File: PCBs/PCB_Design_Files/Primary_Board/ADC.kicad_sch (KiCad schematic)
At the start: 0 parts

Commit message: update
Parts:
- added U10: 74HC595D, symbol project_symbols:74HC595D
- added U11: TMUX1104DGSR, symbol project_symbols:TMUX1104
- added U7: REF3333AIDBZR, symbol project_symbols:REF3333AIDBZR
- added U8: TMUX1133PWR, symbol project_symbols:TMUX1133PWR
- added U9: MCP6561T-E/OT, symbol project_symbols:MCP6561T-E/OT

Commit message: added some parts of schematic
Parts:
- added C10, C11, C12, C13: 10nF, symbol Device:C_Small
- added C14, C53, C54: 100nF, symbol Device:C_Small
- added C15, C16, C17, C18, C19, C20, C21, C22, C23, C24, C25, C26, C27, C28, C29, C33, C34, C35, C36, C37, C38, C39, C40, C41, C42, C43, C44, C45, C46, C47: 8pF, symbol Device:C_Small
- added C30, C48: 4pF, symbol Device:C_Small
- added C31, C49: 2pF, symbol Device:C_Small
- added C32, C50, C51, C52: 1pF, symbol Device:C_Small
- added R12, R13, R14, R15: 100, symbol Device:R_Small_US
- added R16: 10k, symbol Device:R_Small_US
- added SR2: 74HC595D, symbol project_symbols:74HC595D
- added U10: TMUX1133PWR, symbol project_symbols:TMUX1133PWR
- renumbered U10 to SR1
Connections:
- net A0: now reaches U11.1 (A0)
- net A1: now reaches U11.10 (A1)
- net at U11.2 (S1): now also C12.1, R12.2
- net GND: now reaches U11.3 (GND)
- net GND: now also SR1.13 (~{G}), U8.1 (S2B), U8.13 (S1B), U8.3 (S3B), C10.2, C11.2, C12.2, C13.2, C14.2, C52.2, C53.2, C54.2, SR2.13 (~{G}), U10.1 (S2B), U10.13 (S1B), U10.3 (S3B)
- net at U11.4 (S3): now also C10.1, R14.2
- net at U11.5 (EN): now also R16.1
- net +3V3: now reaches U11.6 (VDD)
- net +3V3: now also SR1.10 (~{SCLR}), SR1.16 (VCC), C14.1, C53.1, C54.1, R16.2, SR2.10 (~{SCLR}), SR2.16 (VCC)
- net at U11.7 (S4): now also C13.1, R15.2
- net VSMP: now reaches U11.8 (D)
- net VSMP: now also U8.12 (S1A), U8.2 (S2A), U8.5 (S3A), U10.12 (S1A), U10.2 (S2A), U10.5 (S3A)
- net at U11.9 (S2): now also C11.1, R13.2
- net BIT_12_SEL: now reaches SR1.1 (QB)
- net BIT_12_SEL: now also U8.10 (SEL2), U10.10 (SEL2)
- net sCLK: now reaches SR1.11 (SCK)
- net sCLK: now also SR2.11 (SCK)
- net LATCH: now reaches SR1.12 (RCK)
- net LATCH: now also SR2.12 (RCK)
- net MOSI: now reaches SR1.14 (SI)
- net BIT_13_SEL: now reaches SR1.15 (QA)
- net BIT_13_SEL: now also U8.11 (SEL1), U10.11 (SEL1)
- net BIT_11_SEL: now reaches SR1.2 (QC)
- net BIT_11_SEL: now also U8.9 (SEL3), U10.9 (SEL3)
- net BIT_10_SEL: now reaches SR1.3 (QD)
- net BIT_9_SEL: now reaches SR1.4 (QE)
- net BIT_8_SEL: now reaches SR1.5 (QF)
- net BIT_7_SEL: now reaches SR1.6 (QG)
- net BIT_6_SEL: now reaches SR1.7 (QH)
- net at SR1.9 (QH'): now also SR2.14 (SI)
- net BIT_13_BOT: now reaches U8.14 (D1)
- net BIT_13_BOT: now also C15.2, C16.2, C17.2, C18.2, C19.2, C20.2, C21.2, C22.2, U10.14 (D1)
- net BIT_12_BOT: now reaches U8.15 (D2)
- net BIT_12_BOT: now also C23.2, C24.2, C25.2, C26.2, U10.15 (D2)
- net BIT_11_BOT: now reaches U8.4 (D3)
- net BIT_11_BOT: now also C27.2, C28.2, U10.4 (D3)
- net V_COMP: now reaches U9.1
- net MSB_TOP: now reaches U9.3 (+)
- net MSB_TOP: now also C15.1, C16.1, C17.1, C18.1, C19.1, C20.1, C21.1, C22.1, C23.1, C24.1, C25.1, C26.1, C27.1, C28.1, C29.1, C30.1, C31.1, C32.1, C51.1
- net V_CM: now reaches U9.4 (-)
- new net ADC_Input1: R12.1
- new net ADC_Input2: R13.1
- new net ADC_Input3: R14.1
- new net ADC_Input4: R15.1
- new net BIT_0_BOT: C50.2
- new net BIT_0_SEL: SR2.5 (QF)
- new net BIT_10_BOT: C29.2
- new net BIT_1_BOT: C49.2
- new net BIT_1_SEL: SR2.4 (QE)
- new net BIT_2_BOT: C48.2
- new net BIT_2_SEL: SR2.3 (QD)
- new net BIT_3_BOT: C47.2
- new net BIT_3_SEL: SR2.2 (QC)
- new net BIT_4_BOT: C45.2, C46.2
- new net BIT_4_SEL: SR2.1 (QB)
- new net BIT_5_BOT: C41.2, C42.2, C43.2, C44.2
- new net BIT_5_SEL: SR2.15 (QA)
- new net BIT_6_BOT: C33.2, C34.2, C35.2, C36.2, C37.2, C38.2, C39.2, C40.2
- new net BIT_7_BOT: C32.2
- new net BIT_8_BOT: C31.2
- new net BIT_9_BOT: C30.2
- new net LSB_TOP: C33.1, C34.1, C35.1, C36.1, C37.1, C38.1, C39.1, C40.1, C41.1, C42.1, C43.1, C44.1, C45.1, C46.1, C47.1, C48.1, C49.1, C50.1, C51.2, C52.1
- new net TOP_RESET: SR2.6 (QG)
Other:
- note added: "Bit 0"
- note added: "Bit 1"
- note added: "Bit 10"
- note added: "Bit 11"
- note added: "Bit 12"
- note added: "Bit 13"
- note added: "Bit 2"
- note added: "Bit 3"
- note added: "Bit 4"
- note added: "Bit 5"
- note added: "Bit 6"
- note added: "Bit 7"
- note added: "Bit 8"
- note added: "Bit 9"
- note added: "DAC Capacitors"
- note added: "LSB BRANCH"
- note added: "MSB BRANCH"
- note added: "Termination"
- moved on the sheet: SR1, U11, U8, U9A, U9B

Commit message: ADC schematic done
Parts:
- removed U10: TMUX1133PWR, symbol project_symbols:TMUX1133PWR
- removed U7: REF3333AIDBZR, symbol project_symbols:REF3333AIDBZR
- added C55, C56, C57, C58, C59, C60, C61, C62, C63, C64, C65: 100nF, symbol Device:C_Small
- added U12, U13, U14, U15: TMUX1133PWR, symbol project_symbols:TMUX1133PWR
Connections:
- net ADC_Input4 is gone; now on net +3V3: R15.1
- net +3V3: now also U8.16 (VDD), U9.5 (VDD), C60.1, C61.1, C62.1, C63.1, C64.1, C65.1, U12.16 (VDD), U13.16 (VDD), U14.16 (VDD), U15.16 (VDD)
- net BIT_0_BOT: now also U15.15 (D2)
- net BIT_0_SEL: now also U15.10 (SEL2)
- net BIT_10_BOT: now also U12.14 (D1)
- net BIT_10_SEL: now also U12.11 (SEL1)
- net BIT_1_BOT: now also U15.14 (D1)
- net BIT_1_SEL: now also U15.11 (SEL1)
- net BIT_2_BOT: now also U14.4 (D3)
- net BIT_2_SEL: now also U14.9 (SEL3)
- net BIT_3_BOT: now also U14.15 (D2)
- net BIT_3_SEL: now also U14.10 (SEL2)
- net BIT_4_BOT: now also U14.14 (D1)
- net BIT_4_SEL: now also U14.11 (SEL1)
- net BIT_5_BOT: now also U13.4 (D3)
- net BIT_5_SEL: now also U13.9 (SEL3)
- net BIT_6_BOT: now also U13.15 (D2)
- net BIT_6_SEL: now also U13.10 (SEL2)
- net BIT_7_BOT: now also U13.14 (D1)
- net BIT_7_SEL: now also U13.11 (SEL1)
- net BIT_8_BOT: now also U12.4 (D3)
- net BIT_8_SEL: now also U12.9 (SEL3)
- net BIT_9_BOT: now also U12.15 (D2)
- net BIT_9_SEL: now also U12.10 (SEL2)
- net GND: now also SR1.8 (GND), SR2.8 (GND), U8.6 (~{EN}), U8.8 (GND), U9.4 (VSS), C55.1, C56.1, C57.1, C58.1, C59.1, C60.2, C61.2, C62.2, C63.2, C64.2, C65.2, U12.1 (S2B), U12.13 (S1B), U12.3 (S3B), U12.6 (~{EN}), U12.8 (GND), U13.1 (S2B), U13.13 (S1B), U13.3 (S3B), U13.6 (~{EN}), U13.8 (GND), U14.1 (S2B), U14.13 (S1B), U14.3 (S3B), U14.6 (~{EN}), U14.8 (GND), U15.1 (S2B), U15.13 (S1B), U15.6 (~{EN}), U15.8 (GND)
- net MSB_TOP: now also U15.4 (D3)
- net TOP_RESET: now also U15.9 (SEL3)
- net VSMP: now also U12.12 (S1A), U12.2 (S2A), U12.5 (S3A), U13.12 (S1A), U13.2 (S2A), U13.5 (S3A), U14.12 (S1A), U14.2 (S2A), U14.5 (S3A), U15.12 (S1A), U15.2 (S2A)
- net V_CM: now also U15.5 (S3A)
- net at U8.7 (VSS): now also C55.2
- new net: C56.2, U12.7 (VSS)
- new net: C57.2, U13.7 (VSS)
- new net: C58.2, U14.7 (VSS)
- new net: C59.2, U15.7 (VSS)
- no-connect marks 0 -> 1
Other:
- note added: "4:1 Mux"
- note added: "Output Comp"
- note added: "Serial to Parallel"
- moved on the sheet: C10, C11, C12, C13, C14, C15, C16, C17, C18, C19, C20, C21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

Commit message: updated bom
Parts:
- added C66, C67: 100nF, symbol Device:C_Small
- added U7: REF3333AIDBZR, symbol project_symbols:REF3333AIDBZR
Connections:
- net +3V3: no longer R15.1
- net GND: now also C66.2, C67.2, U7.2 (GND)
- new net +3V3A: C67.1, R15.1, U7.3 (Vout)
- new net +5V: C66.1, U7.1 (Vin)

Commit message: Started Layout
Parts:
- C10, C11, C12, C13, C15, C16, C17, C18, C19, C20, C21, C22, C23, C24, C25, C26, C27, C28, C29, C30, C31, C32, C33, C34, C35, C36, C37, C38, C39, C40, C41, C42, C43, C44, C45, C46, C47, C48, C49, C50, C51, C52: footprint (none) -> Capacitor_SMD:C_0603_1608Metric
- C14, C53, C54, C55, C56, C57, C58, C59, C60, C61, C62, C63, C64, C65: footprint (none) -> Capacitor_SMD:C_0402_1005Metric; Package 0603 -> 0402
- C66, C67: value 100nF -> 1uF; footprint (none) -> Capacitor_SMD:C_0402_1005Metric; Package 0603 -> 0402
- R12, R13, R14, R15, R16: footprint (none) -> Resistor_SMD:R_0402_1005Metric; Package 0603 -> 0402
- SR1, SR2: footprint (none) -> Package_SO:SOIC-16_3.9x9.9mm_P1.27mm
- U11: footprint (none) -> Package_SO:VSSOP-10_3x3mm_P0.5mm
- U12, U13, U14, U15, U8: footprint (none) -> Package_SO:TSSOP-16_4.4x5mm_P0.65mm
- U7: footprint (none) -> Package_TO_SOT_SMD:SOT-23-3
- U9: footprint (none) -> Package_TO_SOT_SMD:SOT-23-5_HandSoldering
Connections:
- net GND: now also U9.2 (VSS); no longer U9.4 (VSS)
- no-connect marks 1 -> 3
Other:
- moved on the sheet: C15, C16, C17, C18, C19, C20, C21, C22, C23, C24, C25, C26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

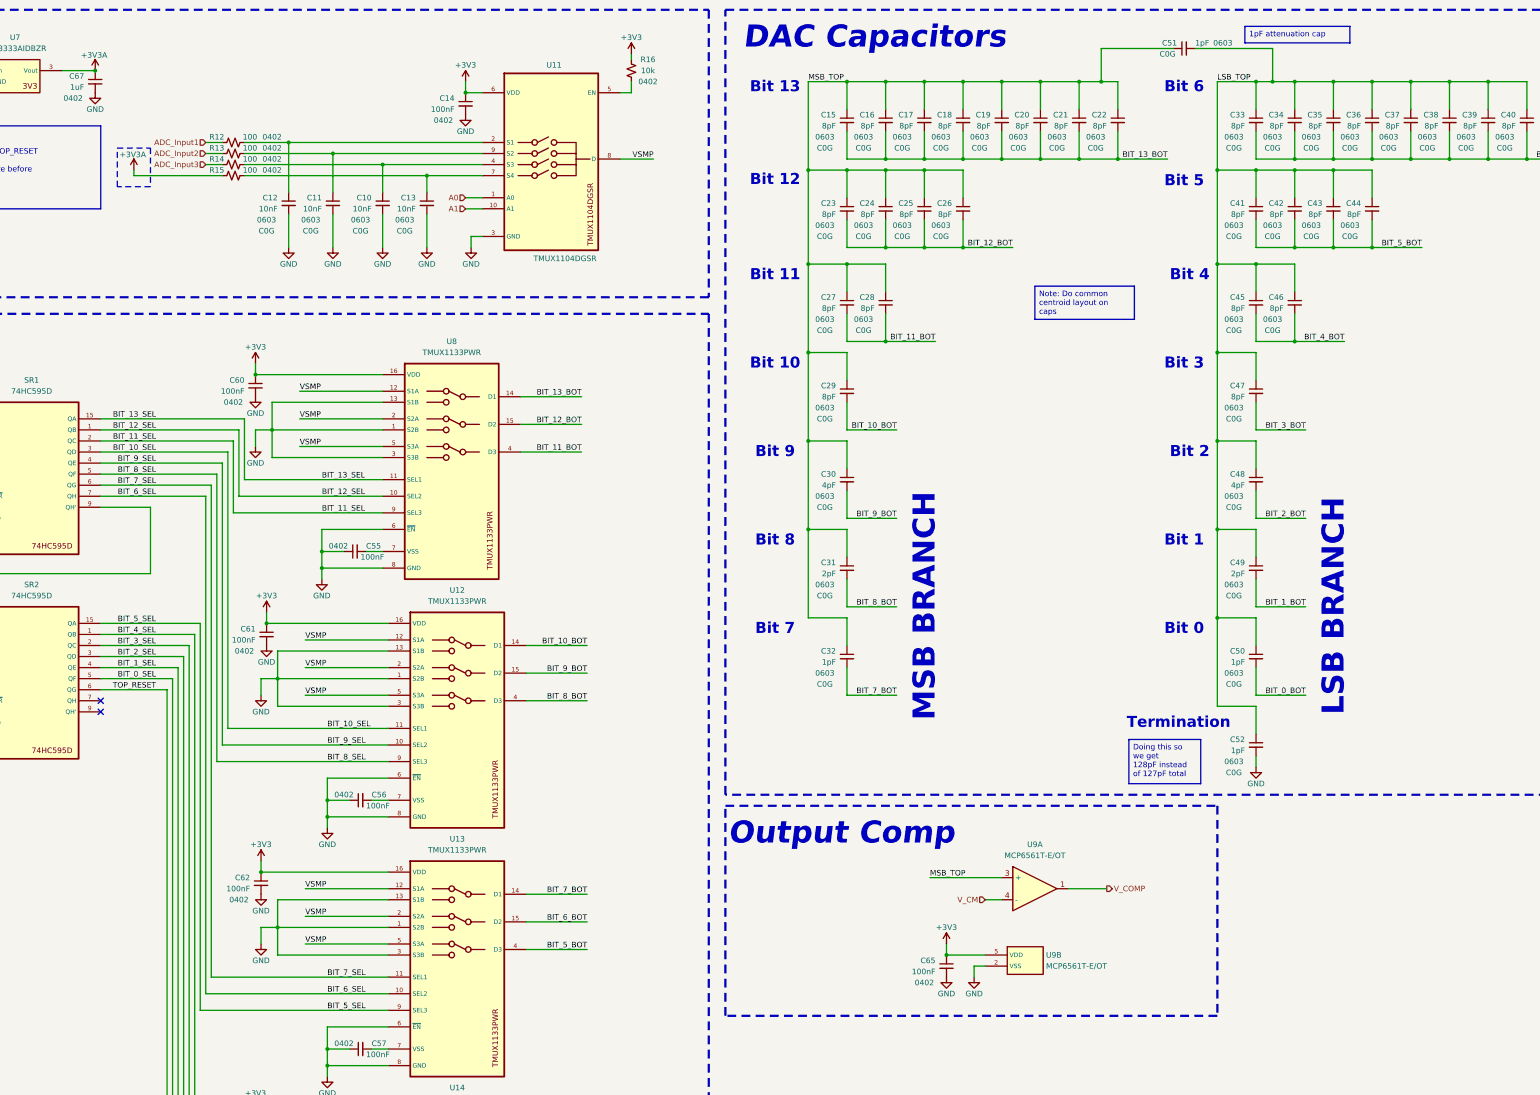
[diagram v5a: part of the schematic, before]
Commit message: added bypass
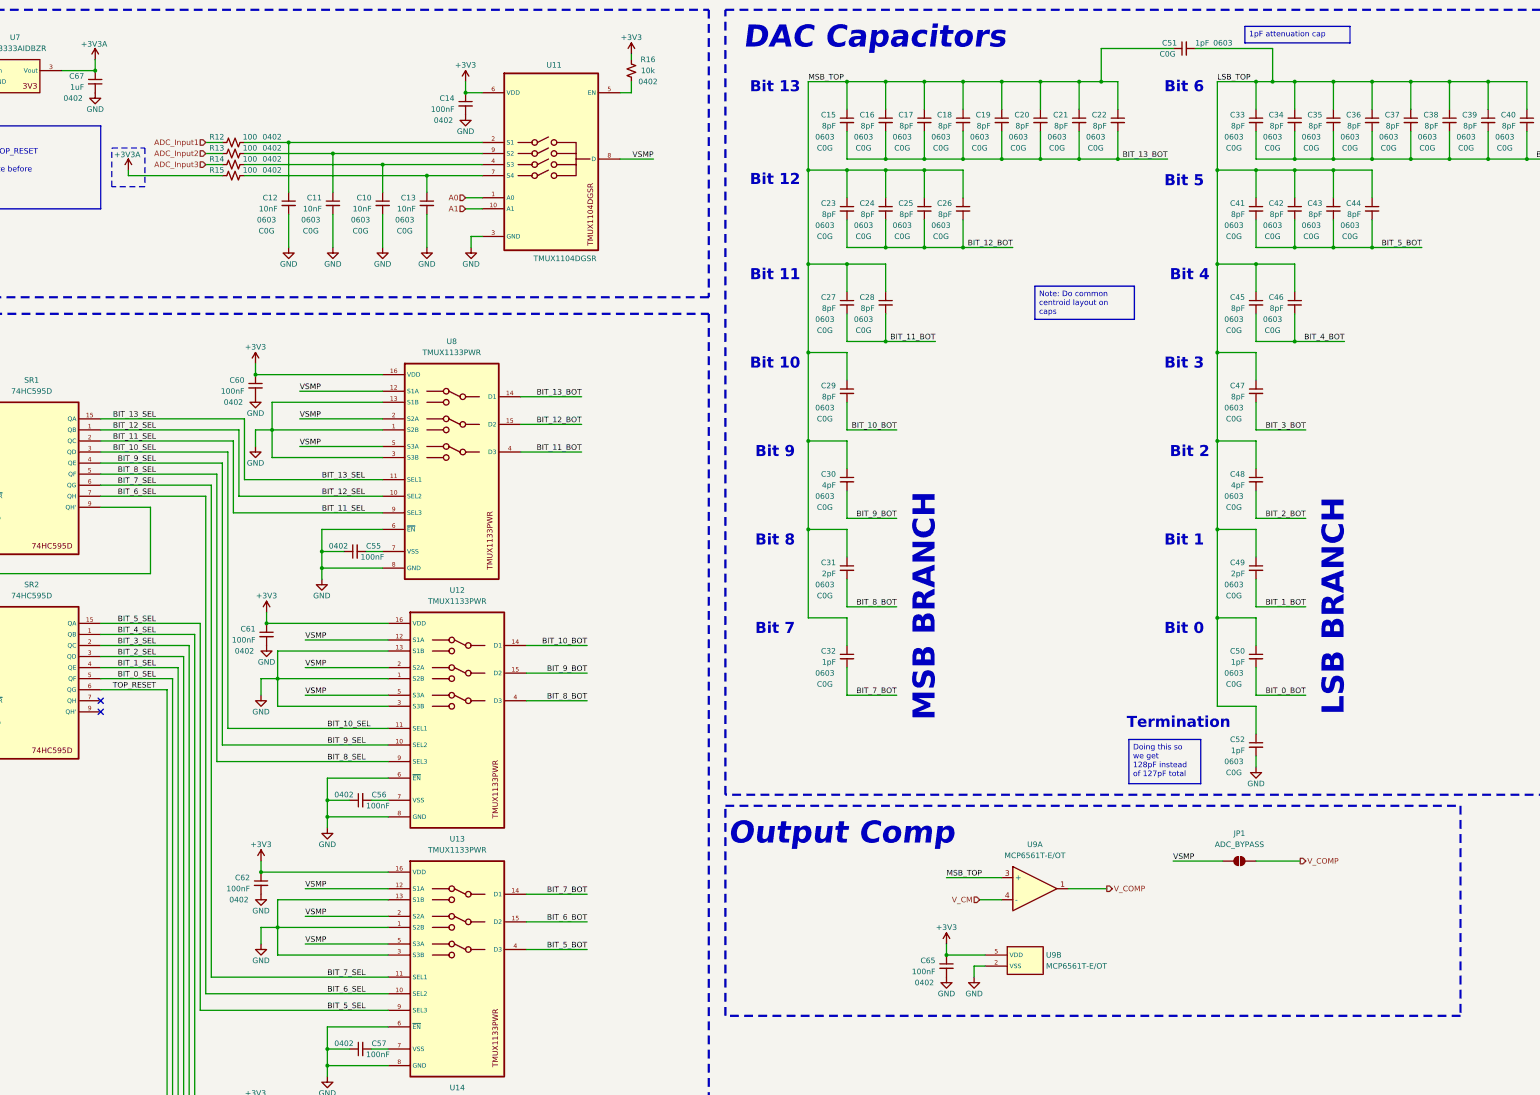
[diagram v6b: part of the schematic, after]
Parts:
- added JP1: ADC_BYPASS, Jumper:SolderJumper-2_P1.3mm_Open_Pad1.0x1.5mm, symbol Jumper:SolderJumper_2_Open
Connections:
- net VSMP: now also JP1.1 (A)
- net V_COMP: now also JP1.2 (B)
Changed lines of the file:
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@@
 	(rectangle
 		(start 270.51 203.2)
-		(end 383.54 251.46)
+		(end 439.42 251.46)
 		(stroke
 			(width 0.508)
@@
 	)
 	(rectangle
-		(start 130.81 52.07)
-		(end 138.43 60.96)
+		(start 129.54 52.07)
+		(end 137.16 60.96)
 		(stroke
 			(width 0.254)
@@
 	(wire
 		(pts
+			(xy 125.73 31.75) (xy 125.73 34.29)
+		)
+		(stroke
+			(width 0)
+			(type default)
+		)
+	)
+	(wire
+		(pts
 			(xy 410.21 68.58) (xy 410.21 74.93)
 		)
@@
 	(wire
 		(pts
-			(xy 134.62 58.42) (xy 154.94 58.42)
+			(xy 133.35 58.42) (xy 154.94 58.42)
 		)
 		(stroke
@@
 	(wire
 		(pts
+			(xy 373.38 215.9) (xy 384.81 215.9)
+		)
+		(stroke
+			(width 0)
+			(type default)
+		)
+	)
+	(wire
+		(pts
 			(xy 146.05 168.91) (xy 146.05 307.34)
 		)
@@
 	(wire
 		(pts
-			(xy 134.62 57.15) (xy 134.62 58.42)
+			(xy 133.35 57.15) (xy 133.35 58.42)
 		)
 		(stroke
@@
 	(wire
 		(pts
+			(xy 392.43 215.9) (xy 402.59 215.9)
+		)
+		(stroke
+			(width 0)
+			(type default)
+		)
+	)
+	(wire
+		(pts
 			(xy 289.56 99.06) (xy 289.56 78.74)
 		)
@@
 	(wire
 		(pts
-			(xy 317.5 219.71) (xy 334.01 219.71)
+			(xy 321.31 219.71) (xy 334.01 219.71)
 		)
 		(stroke
@@
 	(wire
 		(pts
-			(xy 330.2 224.79) (xy 334.01 224.79)
+			(xy 328.93 224.79) (xy 334.01 224.79)
 		)
 		(stroke
@@
 		)
 	)
+	(label "VSMP"
+		(at 373.38 215.9 0)
+		(effects
+			(font
+				(size 1.27 1.27)
+			)
+			(justify left bottom)
+		)
+	)
 	(label "BIT_0_BOT"
 		(at 403.86 177.8 180)
@@
 	)
 	(label "MSB_TOP"
-		(at 317.5 219.71 0)
+		(at 321.31 219.71 0)
 		(effects
 			(font
@@
 		)
 	)
+	(hierarchical_label "V_COMP"
+		(shape output)
+		(at 402.59 215.9 0)
+		(effects
+			(font
+				(size 1.27 1.27)
+			)
+			(justify left)
+		)
+	)
 	(hierarchical_label "V_CM"
 		(shape input)
-		(at 330.2 224.79 180)
+		(at 328.93 224.79 180)
 		(effects
 			(font
@@
 	(symbol
 		(lib_id "power:+3V3")
-		(at 134.62 57.15 0)
+		(at 133.35 57.15 0)
 		(unit 1)
 		(exclude_from_sim no)
@@
 		(dnp no)
 		(property "Reference" "#PWR066"
-			(at 134.62 60.96 0)
+			(at 133.35 60.96 0)
 			(effects
 				(font
@@
 		)
 		(property "Value" "+3V3A"
-			(at 134.366 53.594 0)
+			(at 133.096 53.594 0)
 			(effects
 				(font
@@
 		)
 		(property "Footprint" ""
-			(at 134.62 57.15 0)
+			(at 133.35 57.15 0)
 			(effects
 				(font
@@
 		)
 		(property "Datasheet" ""
-			(at 134.62 57.15 0)
+			(at 133.35 57.15 0)
 			(effects
 				(font
@@
 		)
 		(property "Description" "Power symbol creates a global label with name \"+3V3\""
-			(at 134.62 57.15 0)
+			(at 133.35 57.15 0)
 			(effects
 				(font
@@
 	(symbol
 		(lib_id "power:+3V3")
-		(at 125.73 34.29 0)
+		(at 125.73 31.75 0)
 		(unit 1)
 		(exclude_from_sim no)
@@
 		(dnp no)
 		(property "Reference" "#PWR073"
-			(at 125.73 38.1 0)
+			(at 125.73 35.56 0)
 			(effects
 				(font
@@
 		)
 		(property "Value" "+3V3A"
-			(at 125.476 30.734 0)
+			(at 125.476 28.194 0)
 			(effects
 				(font
@@
 		)
 		(property "Footprint" ""
-			(at 125.73 34.29 0)
+			(at 125.73 31.75 0)
 			(effects
 				(font
@@
 		)
 		(property "Datasheet" ""
-			(at 125.73 34.29 0)
+			(at 125.73 31.75 0)
 			(effects
 				(font
@@
 		)
 		(property "Description" "Power symbol creates a global label with name \"+3V3\""
-			(at 125.73 34.29 0)
+			(at 125.73 31.75 0)
 			(effects
 				(font
@@
 					(unit 1)
 				)
+			)
+		)
+	)
+	(symbol
+		(lib_id "Jumper:SolderJumper_2_Open")
+		(at 388.62 215.9 0)
+		(unit 1)
+		(exclude_from_sim no)
+		(in_bom no)
+		(on_board yes)
+		(dnp no)
+		(fields_autoplaced yes)
+		(property "Reference" "JP1"
+			(at 388.62 209.55 0)
+			(effects
+				(font
+					(size 1.27 1.27)
+				)
+			)
+		)
+		(property "Value" "ADC_BYPASS"
+			(at 388.62 212.09 0)
+			(effects
+				(font
+					(size 1.27 1.27)
+				)
+			)
+		)
+		(property "Footprint" "Jumper:SolderJumper-2_P1.3mm_Open_Pad1.0x1.5mm"
+			(at 388.62 215.9 0)
+			(effects
+				(font
+					(size 1.27 1.27)
+				)
+				(hide yes)
+			)
+		)
+		(property "Datasheet" "~"
+			(at 388.62 215.9 0)
+			(effects
+				(font
+					(size 1.27 1.27)
+				)
+				(hide yes)
+			)
+		)
+		(property "Description" "Solder Jumper, 2-pole, open"
+			(at 388.62 215.9 0)
+			(effects
+				(font
+					(size 1.27 1.27)
+				)
+				(hide yes)
+			)
+		)
+		(pin "2"
+		)
+		(pin "1"
+		)
+		(instances
+			(project ""
+				(path "/8c3d01e8-a984-4e4e-9220-7d351336a99b/bd61ebda-1522-4e1f-a5c5-93272ab69f44"
+					(reference "JP1")
+					(unit 1)
+				)
